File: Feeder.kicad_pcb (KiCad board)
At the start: 4 copper layers, 91 x 85 mm, 160 parts, among them J101 Conn_02x03_Odd_Even, J102 Conn_01x03_Pin, Q201 2N7002, Q301 2N7002, Q401 2N7002, Q501 2N7002, Q901 BC857BS, Q902 AO3401A, Q903 BC857BS, Q904 AO3401A, U101 XBLW 24C02S(XBLW), U201 CMP6793RE, U301 CMP6793RE, U401 LM5169PDDAR, U501 LM5169PDDAR, U601 TPS562202, U701 TPS562202, U801 CMP6793RE

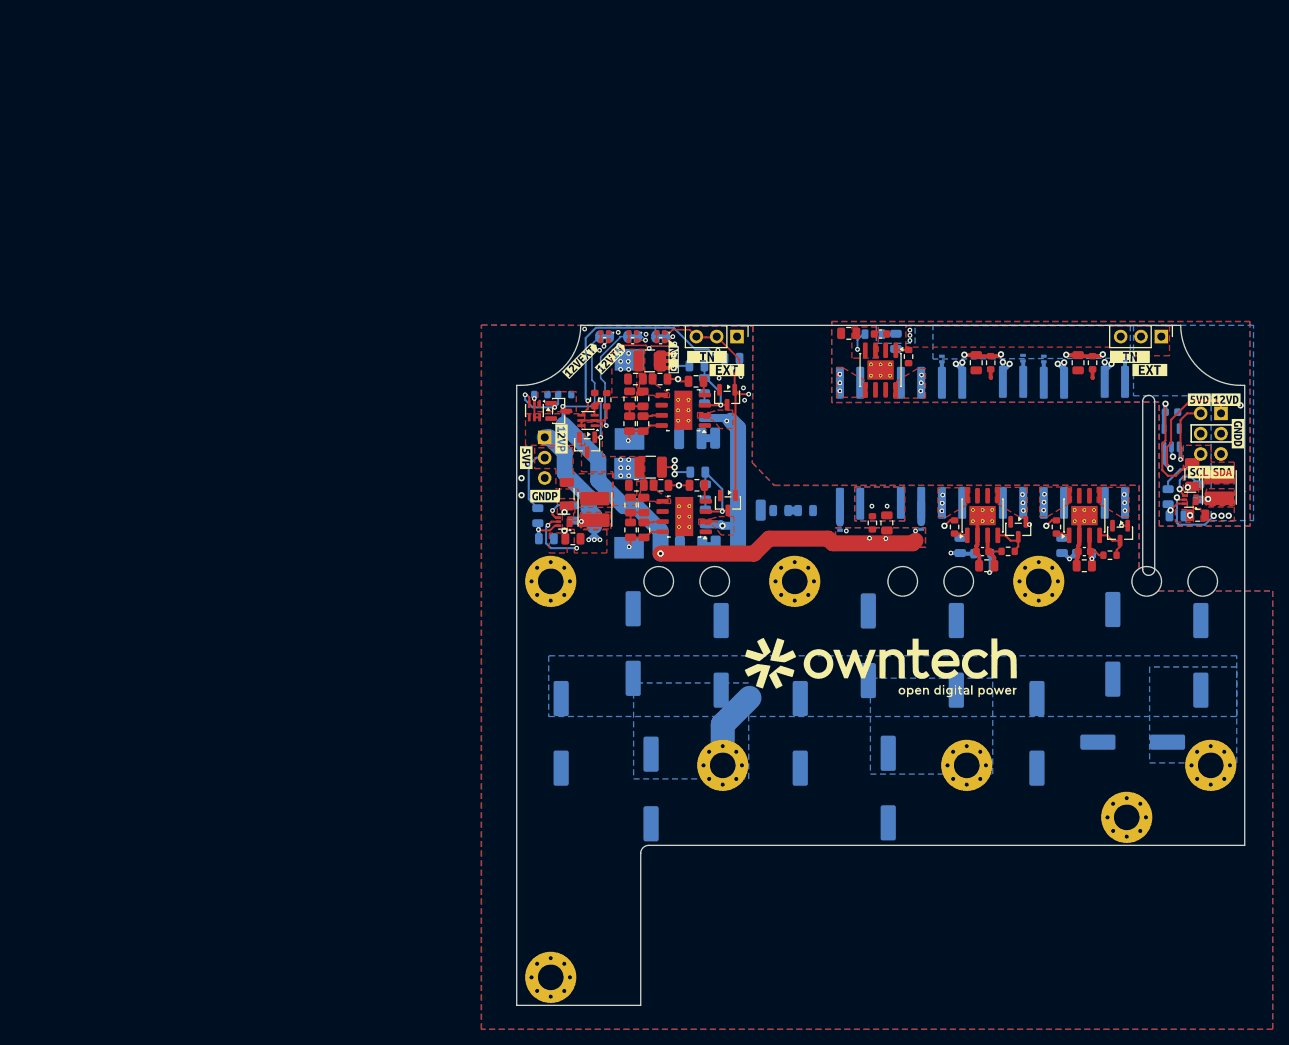
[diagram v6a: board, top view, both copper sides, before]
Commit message: added propoer filter and rerouted filters + enhancements all arround the board. no drc errors except soic8 isolation
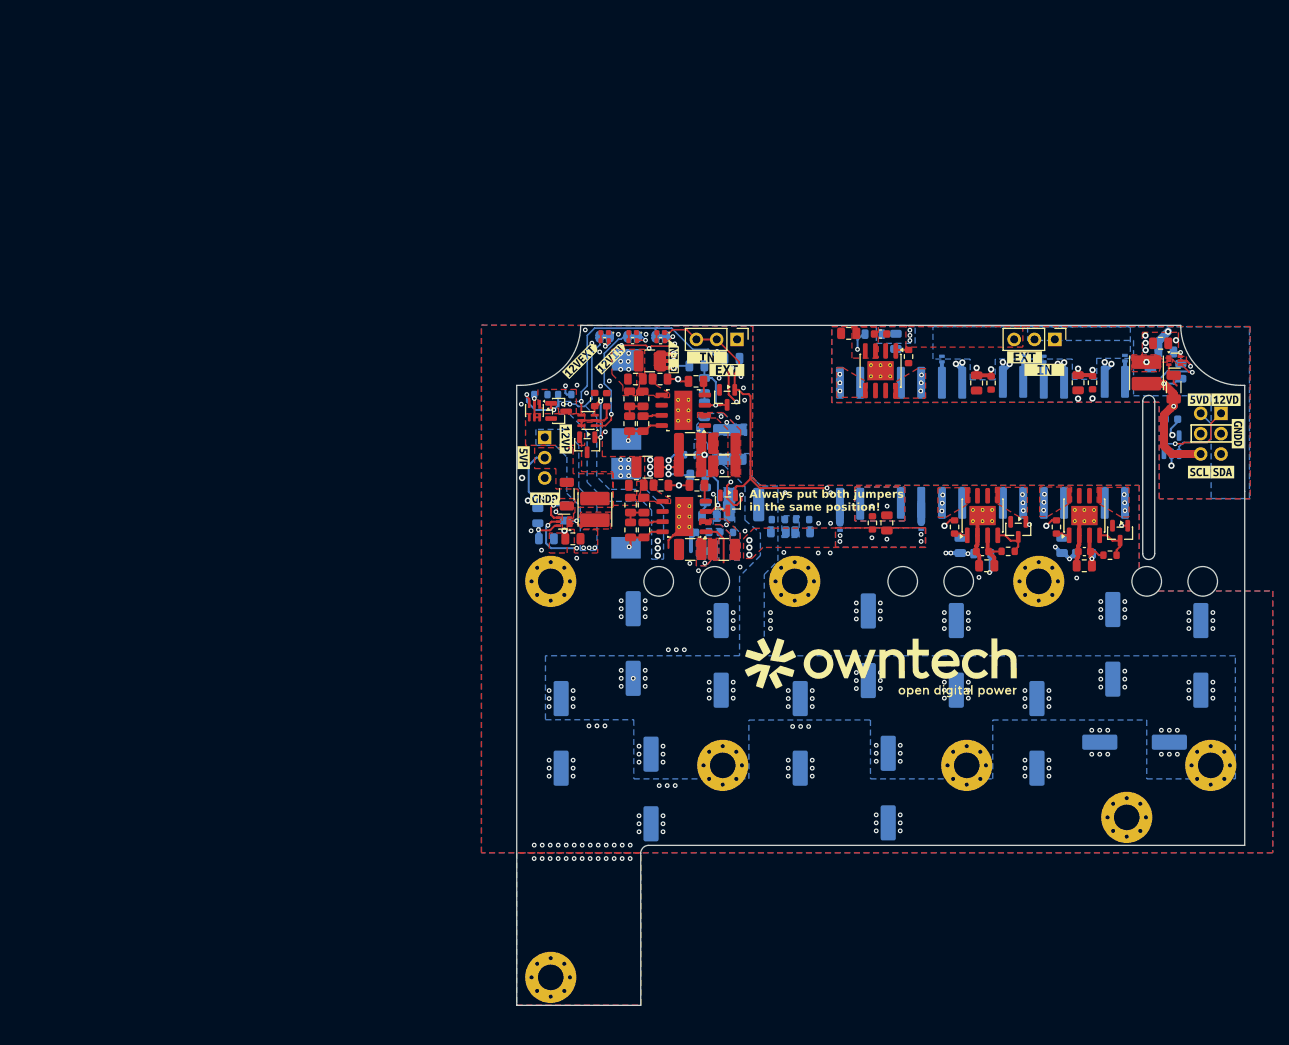
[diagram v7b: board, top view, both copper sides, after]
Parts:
- removed ? (x6): , 
- removed C103, C104, C105, C106: 4.7uF, Footprints:C_1210_3225Metric
- removed L101: 10uH, Inductor_SMD:L_1210_3225Metric
- added C405: 4.7u, Footprints:C_1210_3225Metric, F.Cu at (30.4, -80.2)
- added C406: 4.7u, Footprints:C_1210_3225Metric, F.Cu at (26.2, -77.4)
- added C407: 4.7u, Footprints:C_1210_3225Metric, F.Cu at (30.4, -77.4)
- added C408: 4.7u, Footprints:C_1210_3225Metric, F.Cu at (26.2, -80.2)
- added C505: 4.7u, Footprints:C_1210_3225Metric, F.Cu at (30.4, -67.0)
- added C506: 4.7u, Footprints:C_1210_3225Metric, F.Cu at (26.2, -67.0)
- added C507: 4.7u, Footprints:C_1210_3225Metric, B.Cu at (30.4, -67.0)
- added C508: 4.7u, Footprints:C_1210_3225Metric, B.Cu at (26.2, -67.0)
- added H109: MountingHole, Footprints:Hole_signal_bottom_board_lookup, F.Cu at (22.2, -63.0)
- added H110: MountingHole, Footprints:Hole_signal_bottom_board_lookup, F.Cu at (29.2, -63.0)
- added H111: MountingHole, Footprints:Hole_signal_bottom_board_lookup, F.Cu at (52.8, -63.0)
- added H112: MountingHole, Footprints:Hole_signal_bottom_board_lookup, F.Cu at (59.8, -63.0)
- added H113: MountingHole, Footprints:Hole_signal_bottom_board_lookup, F.Cu at (83.2, -63.0)
- added H114: MountingHole, Footprints:Hole_signal_bottom_board_lookup, F.Cu at (90.2, -63.0)
- added L402: 10u, Inductor_SMD:L_Changjiang_FNR5040S, B.Cu at (31.1, -80.1)
- added L502: 10u, Inductor_SMD:L_Changjiang_FNR5040S, B.Cu at (32.9, -72.6)
- added R102: 2.2M, Resistor_SMD:R_0603_1608Metric, B.Cu at (37.2, -70.7)
- added R103: 2.2M, Resistor_SMD:R_0603_1608Metric, B.Cu at (40.2, -70.7)
- added R408: 2.2M, Resistor_SMD:R_0603_1608Metric, B.Cu at (27.5, -81.2)
- added R409: 2.2M, Resistor_SMD:R_0603_1608Metric, B.Cu at (26.2, -78.8)
- added R508: 2.2M, Resistor_SMD:R_0603_1608Metric, B.Cu at (30.7, -69.1)
- added R509: 2.2M, Resistor_SMD:R_0603_1608Metric, B.Cu at (27.8, -69.1)
- C107, C108, C109, C110, C111, C112, C113, C114, C115, C116, C117, C118: value C_Polarized_US -> 22u
- moved C601 22.0 mm to (85.0, -92.8), turned to 0 degrees
- moved R602 20.5 mm to (85.7, -91.7), turned to 180 degrees
- moved U601 17.5 mm to (86.7, -90.6), turned to 0 degrees
- moved L601 17.0 mm to (83.2, -89.1), turned to -90 degrees
- moved R601 15.8 mm to (87.5, -89.3), turned to 90 degrees
- moved kibuzzard-6A957D2D 15.7 mm to (68.0, -91.0)
- moved C602 15.7 mm to (83.7, -88.7), turned to 90 degrees
- moved JP101 13.3 mm to (71.8, -93.2)
- moved C603 11.2 mm to (86.6, -87.3), turned to 90 degrees
- moved kibuzzard-6A957D3B 10.8 mm to (70.5, -89.4)
- moved C102 2.69 mm to (40.2, -69.2)
- moved C101 2.68 mm to (37.2, -69.2)
- moved C304 2.53 mm to (62.0, -87.8)
- moved R304 2.53 mm to (63.8, -87.8)
- moved C204 2.50 mm to (74.7, -87.8)
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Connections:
- JP101 pad 1: /dc-dc_isolated/VIN -> /dc-dc_isolated_disabling/VOUT
- JP101 pad 3: /dc-dc_isolated_disabling/VOUT -> /dc-dc_isolated/VIN
- R406 pad 1: /VIN_{FILT} -> /buck/VIN_{FILT}
- R506 pad 1: /VIN_{FILT} -> /buck1/VIN_{FILT}
- U401 pad 2: /VIN_{FILT} -> /buck/VIN_{FILT}
- U501 pad 2: /VIN_{FILT} -> /buck1/VIN_{FILT}
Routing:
- net /12V_DIGI_TO_POWER: track 72.3 -> 12.3 mm, vias 6 -> 14
- net PGND: track 47.4 -> 79.8 mm, vias 31 -> 165
- net /VIN_{FILT}: track 25.2 -> 0.00 mm, vias 2 -> 0
- net +12V_PGND: track 57.5 -> 39.0 mm
- net /buck/~{EN}: track 101.3 -> 91.0 mm
- net /VHigh: track 9.83 -> 0.00 mm, vias 0 -> 86
- net /SDA: track 18.1 -> 10.9 mm
- net DGND: track 24.1 -> 30.9 mm, vias 12 -> 14
- net +12V_DGND: track 9.40 -> 3.42 mm
- net Net-(C103-Pad2): track 3.41 -> 0.00 mm
- net /buck/VIN_{FILT}: track 0.00 -> 2.80 mm, vias 0 -> 2
- net Net-(U601-VBST): track 5.11 -> 7.82 mm
- net /dc-dc_isolated_disabling/VOUT: track 9.48 -> 7.11 mm
- net Net-(C505-Pad2): track 0.00 -> 1.41 mm, vias 0 -> 1
- net Net-(C101-Pad2): track 1.23 -> 0.00 mm
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- added copper zone on In1.Cu, net +12V_DGND
- added copper zone on In2.Cu, net +12V_DGND
- added copper zone on B.Cu, net +12V_PGND
- added copper zone on In2.Cu, net /12V_DIGI_TO_POWER
- added copper zone on F.Cu, net /VHigh
- added copper zone on B.Cu, net /buck/VIN_{FILT}
- added copper zone on F.Cu, net /buck/VIN_{FILT}
- added copper zone on B.Cu, net /buck1/VIN_{FILT}
- added copper zone on F.Cu, net /buck1/VIN_{FILT}
- added copper zone on B.Cu, net Net-(C101-Pad2)
- added copper zone on B.Cu, net Net-(C405-Pad2)
- added copper zone on F.Cu, net Net-(C405-Pad2)
- added copper zone on B.Cu, net Net-(C505-Pad2)
- added copper zone on F.Cu, net Net-(C505-Pad2)
- removed copper zone on F.Cu, net +5V_DGND
- removed copper zone on F.Cu, net /VIN_{FILT}
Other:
- outline, holes or cut-outs redrawn
- board text added: "Always put both jumpers in the same position!"
